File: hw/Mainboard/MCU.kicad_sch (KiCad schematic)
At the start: 34 parts, among them J25 MENU, SW4 RUN, SW5 MENU, U21 RP2040, Y1 12 MHz

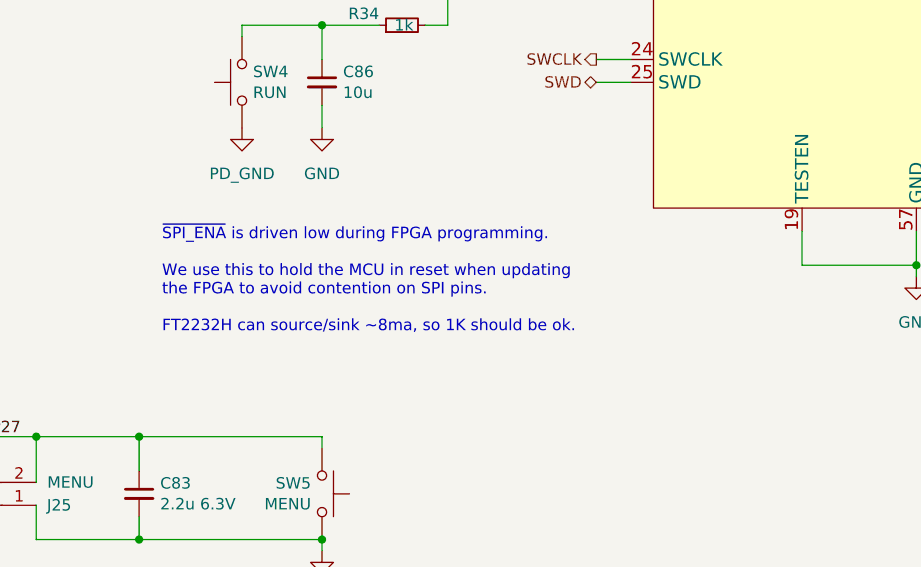
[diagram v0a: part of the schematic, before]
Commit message: docs(hw): SPI0_CSn must be driven low during JTAG programming
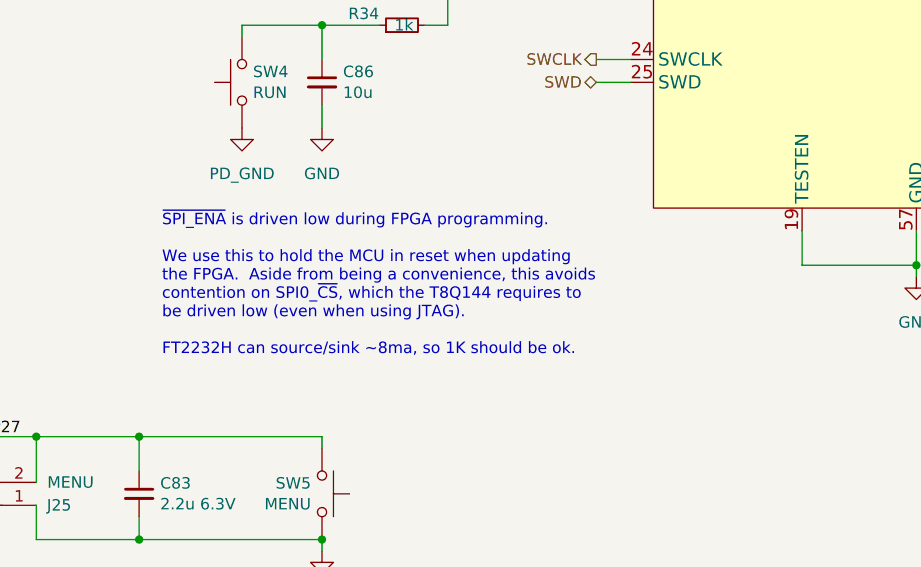
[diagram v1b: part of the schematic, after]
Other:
- note added: "~{SPI_ENA} is driven low during FPGA programming. We use this to hold the MCU in reset when updating the FPGA. Aside from being a convenience, this avoids contention on SPI0_~{CS}, which the T8Q144 requires to be driven low (even when using JTAG). FT2232H can source/sink ~8ma, so 1K should be ok."
- note removed: "~{SPI_ENA} is driven low during FPGA programming. We use this to hold the MCU in reset when updating the FPGA to avoid contention on SPI pins. FT2232H can source/sink ~8ma, so 1K should be ok."
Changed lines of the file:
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@@
     (effects (font (size 1.27 1.27)) (justify left bottom))
   )
-  (text "~{SPI_ENA} is driven low during FPGA programming.\n\nWe use this to hold the MCU in reset when updating\nthe FPGA to avoid contention on SPI pins.\n\nFT2232H can source/sink ~8ma, so 1K should be ok.\n"
-    (at 44.45 149.86 0)
+  (text "~{SPI_ENA} is driven low during FPGA programming.\n\nWe use this to hold the MCU in reset when updating\nthe FPGA.  Aside from being a convenience, this avoids\ncontention on SPI0_~{CS}, which the T8Q144 requires to\nbe driven low (even when using JTAG).\n\nFT2232H can source/sink ~8ma, so 1K should be ok.\n"
+    (at 44.45 152.4 0)
     (effects (font (size 1.27 1.27)) (justify left bottom))
   )
